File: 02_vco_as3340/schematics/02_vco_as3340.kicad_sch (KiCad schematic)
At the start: 23 parts, among them J1 FM IN, J10 Outputs, J11 SQUARE OUT, J12 SAW OUT, J13 TRIANGLE OUT, J14 SINE OUT, J2 PWM CV IN, J3 SYNC IN, J4 1VO IN, J5 Tuning, J6 Sync Mode, J7 FM & PWM, J8 Mode Switch, J9 Panel Power, SW1 SW_Rotary_1x4, SW2 SW_SPDT

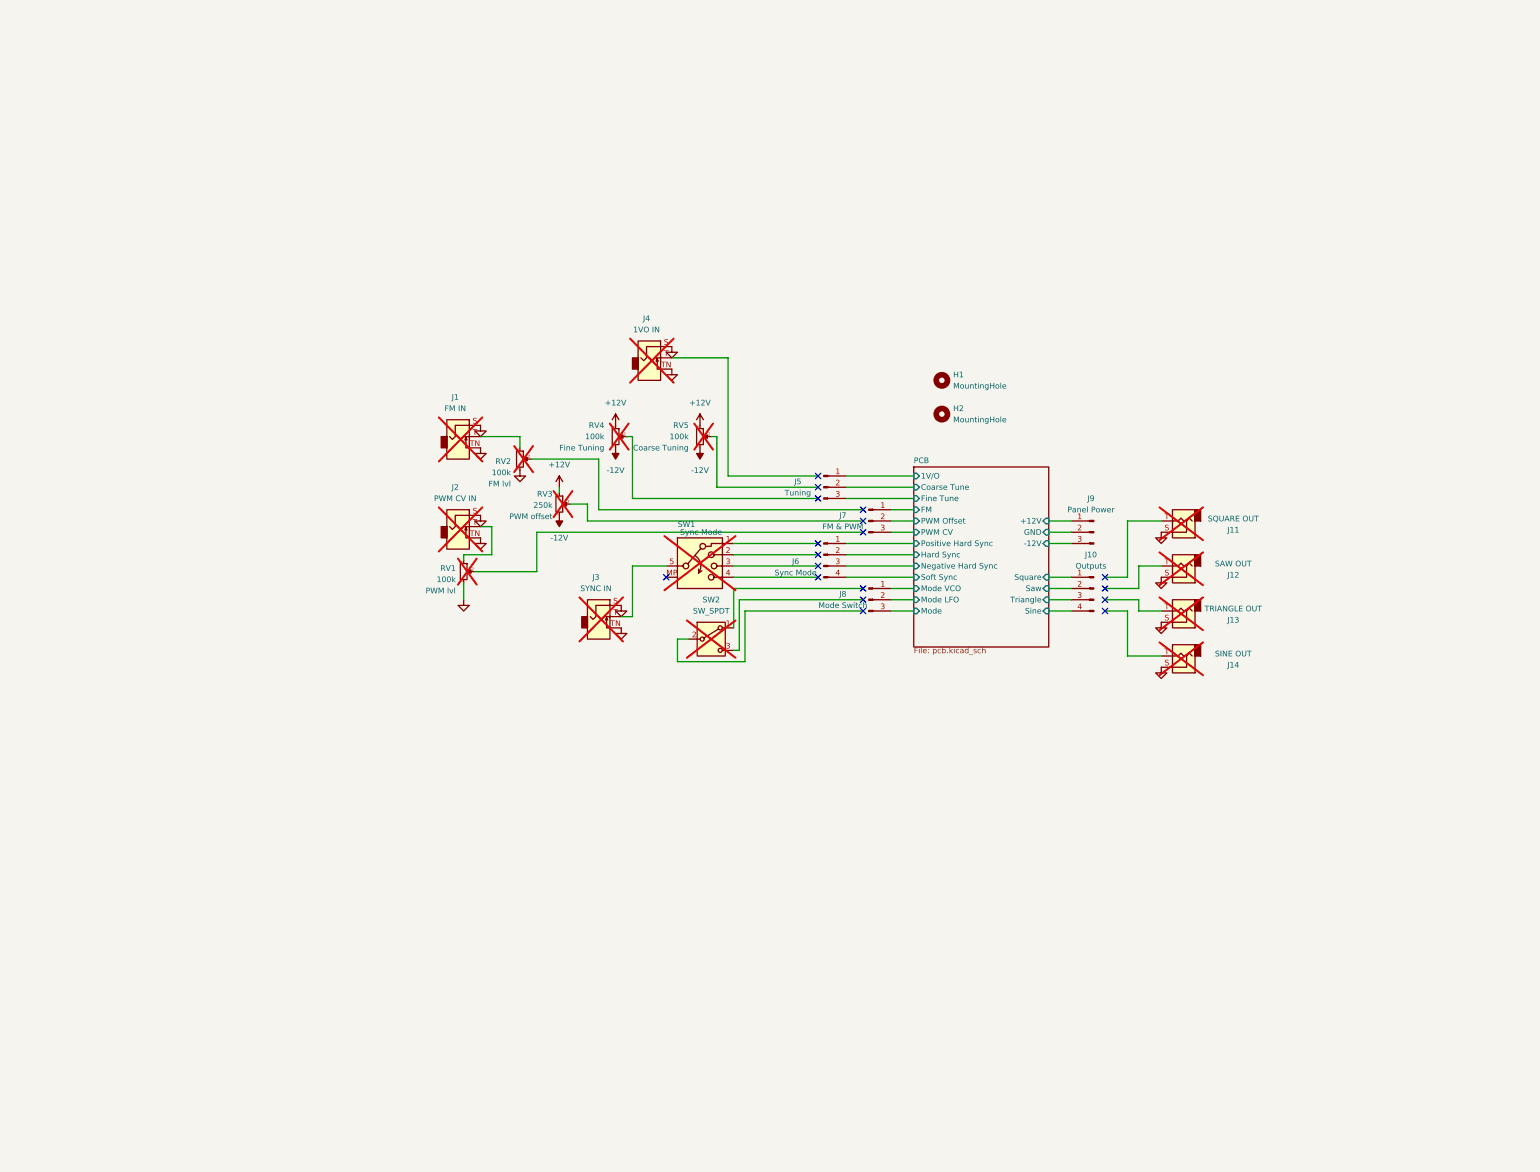
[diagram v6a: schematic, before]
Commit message: split 02 into subboard
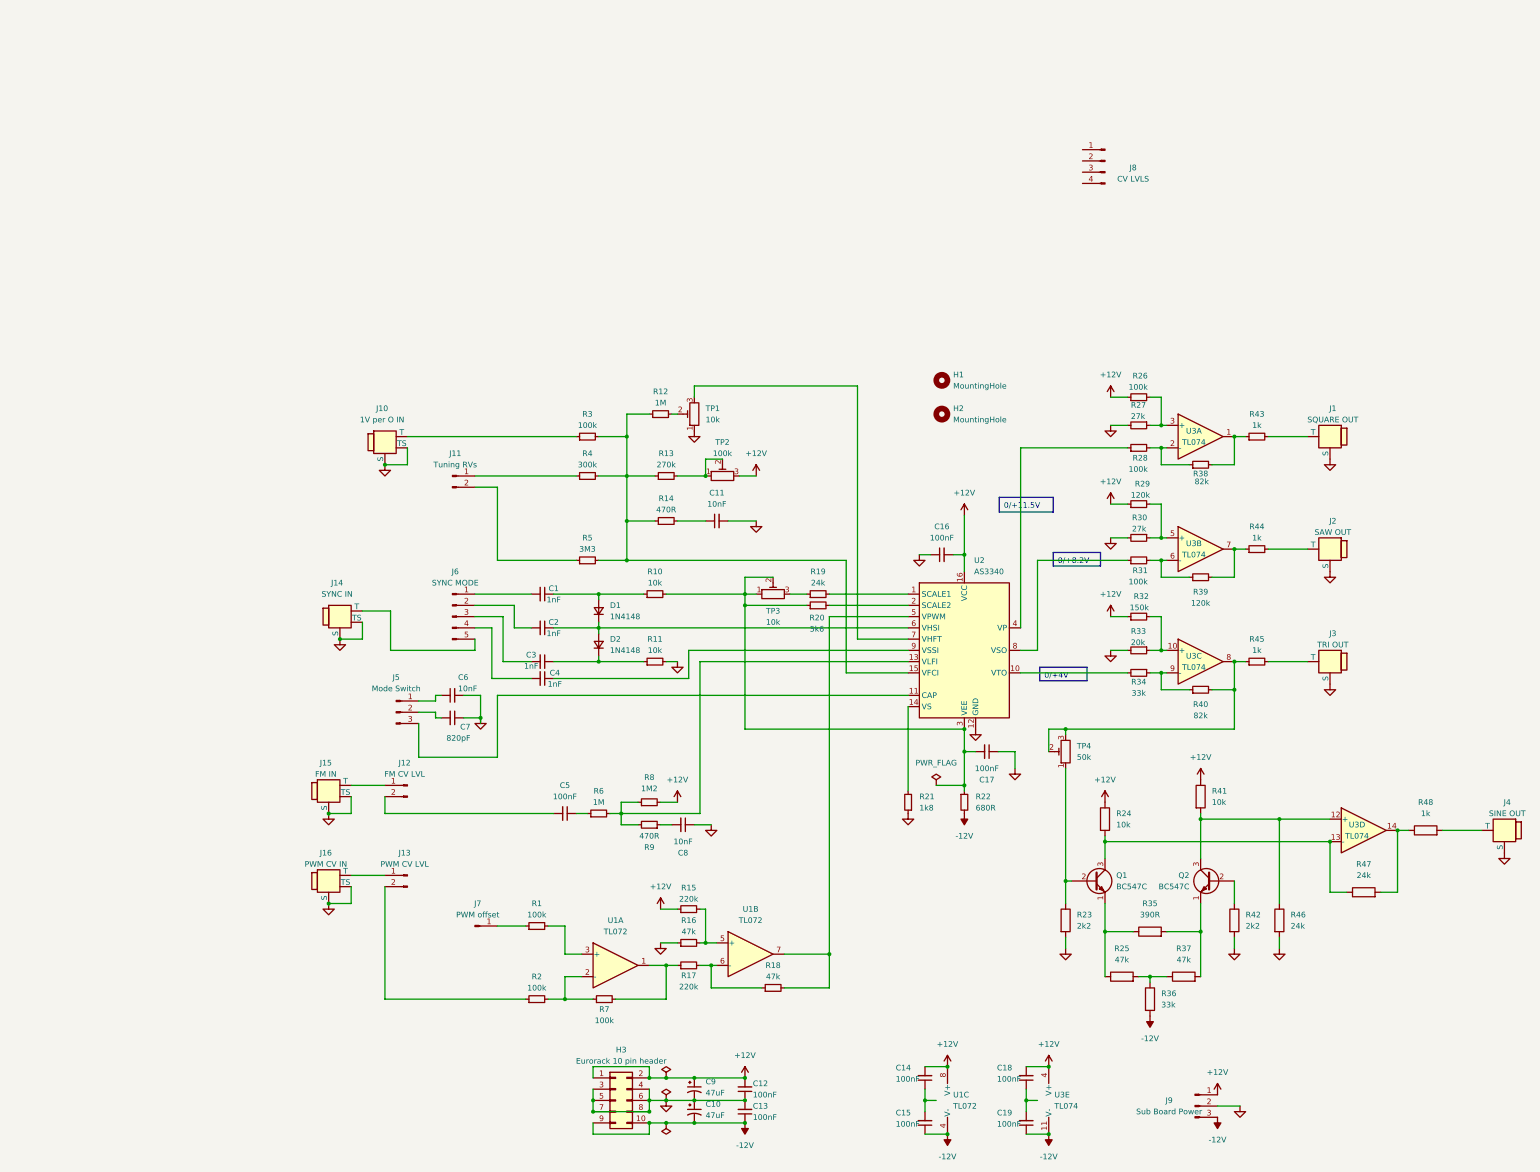
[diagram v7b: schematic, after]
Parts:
- removed J1: FM IN, symbol Connector_Audio:AudioJack2_SwitchT
- removed J10: Outputs, Connector_PinHeader_2.54mm:PinHeader_1x04_P2.54mm_Vertical, symbol Connector:Conn_01x04_Pin
- removed J11: SQUARE OUT, symbol Connector_Audio:AudioJack2
- removed J12: SAW OUT, symbol Connector_Audio:AudioJack2
- removed J13: TRIANGLE OUT, symbol Connector_Audio:AudioJack2
- removed J14: SINE OUT, symbol Connector_Audio:AudioJack2
- removed J2: PWM CV IN, symbol Connector_Audio:AudioJack2_SwitchT
- removed J3: SYNC IN, symbol Connector_Audio:AudioJack2_SwitchT
- removed J4: 1VO IN, symbol Connector_Audio:AudioJack2_SwitchT
- removed J6: Sync Mode, Connector_PinHeader_2.54mm:PinHeader_1x04_P2.54mm_Vertical, symbol Connector:Conn_01x04_Pin
- removed J7: FM & PWM, Connector_PinHeader_2.54mm:PinHeader_1x03_P2.54mm_Vertical, symbol Connector:Conn_01x03_Pin
- removed J8: Mode Switch, Connector_PinHeader_2.54mm:PinHeader_1x03_P2.54mm_Vertical, symbol Connector:Conn_01x03_Pin
- removed RV1, RV2, RV4, RV5: 100k, symbol Device:R_Potentiometer_Small
- removed RV3: 250k, symbol Device:R_Potentiometer_Small
- removed SW1: SW_Rotary_1x4, symbol Switch:SW_Rotary_1x4_MP
- removed SW2: SW_SPDT, symbol Switch:SW_SPDT
- added C1, C2, C3, C4: 1nF, Capacitor_THT:C_Disc_D6.0mm_W2.5mm_P5.00mm, symbol Device:C_Small
- added C10, C9: 47uF, Capacitor_THT:CP_Radial_D6.3mm_P2.50mm, symbol Device:C_Polarized_Small_US
- added C11, C6, C8: 10nF, Capacitor_THT:C_Disc_D6.0mm_W2.5mm_P5.00mm, symbol Device:C_Small
- added C12, C13, C14, C15, C16, C17, C18, C19, C5: 100nF, Capacitor_THT:C_Disc_D6.0mm_W2.5mm_P5.00mm, symbol Device:C_Small
- added C7: 820pF, Capacitor_THT:C_Disc_D6.0mm_W2.5mm_P5.00mm, symbol Device:C_Small
- added D1, D2: 1N4148, Diode_THT:D_DO-35_SOD27_P7.62mm_Horizontal, symbol Device:D_Small
- added H3: Eurorack 10 pin header, Connector_PinHeader_2.54mm:PinHeader_2x05_P2.54mm_Vertical, symbol Connector_Generic:Conn_02x05_Odd_Even
- added J1: SQUARE OUT, cynthia:6.35 mm jack socket mono, symbol cynthia:6.35_mm_jack_socket_mono
- added J10: 1V per O IN, symbol cynthia:6.35_mm_jack_socket_mono_switched
- added J11: Tuning RVs, Connector_PinHeader_2.54mm:PinHeader_1x02_P2.54mm_Vertical, symbol Connector:Conn_01x02_Pin
- added J12: FM CV LVL, Connector_PinHeader_2.54mm:PinHeader_1x02_P2.54mm_Vertical, symbol Connector:Conn_01x02_Pin
- added J13: PWM CV LVL, Connector_PinHeader_2.54mm:PinHeader_1x02_P2.54mm_Vertical, symbol Connector:Conn_01x02_Pin
- added J14: SYNC IN, symbol cynthia:6.35_mm_jack_socket_mono_switched
- added J15: FM IN, symbol cynthia:6.35_mm_jack_socket_mono_switched
- added J16: PWM CV IN, symbol cynthia:6.35_mm_jack_socket_mono_switched
- added J2: SAW OUT, cynthia:6.35 mm jack socket mono, symbol cynthia:6.35_mm_jack_socket_mono
- added J3: TRI OUT, cynthia:6.35 mm jack socket mono, symbol cynthia:6.35_mm_jack_socket_mono
- added J4: SINE OUT, cynthia:6.35 mm jack socket mono, symbol cynthia:6.35_mm_jack_socket_mono
- added J6: SYNC MODE, Connector_PinHeader_2.54mm:PinHeader_1x05_P2.54mm_Vertical, symbol Connector:Conn_01x05_Pin
- added J7: PWM offset, Connector_PinHeader_2.54mm:PinHeader_1x01_P2.54mm_Vertical, symbol Connector:Conn_01x01_Pin
- added J8: CV LVLS, Connector_PinHeader_2.54mm:PinHeader_1x04_P2.54mm_Vertical, symbol Connector:Conn_01x04_Pin
- added Q1, Q2: BC547C, Package_TO_SOT_THT:TO-92_Inline, symbol Transistor_BJT:2N3904
- added R1, R2, R26, R28, R3, R31, R7: 100k, Resistor_THT:R_Axial_DIN0207_L6.3mm_D2.5mm_P10.16mm_Horizontal, symbol Device:R_Small
- added R10, R11: 10k, Resistor_THT:R_Axial_DIN0207_L6.3mm_D2.5mm_P10.16mm_Horizontal, symbol Device:R_Small
- added R12, R6: 1M, Resistor_THT:R_Axial_DIN0207_L6.3mm_D2.5mm_P10.16mm_Horizontal, symbol Device:R_Small
- added R13: 270k, Resistor_THT:R_Axial_DIN0207_L6.3mm_D2.5mm_P10.16mm_Horizontal, symbol Device:R_Small
- added R14, R9: 470R, Resistor_THT:R_Axial_DIN0207_L6.3mm_D2.5mm_P10.16mm_Horizontal, symbol Device:R_Small
- added R15, R17: 220k, Resistor_THT:R_Axial_DIN0207_L6.3mm_D2.5mm_P10.16mm_Horizontal, symbol Device:R_Small
- added R16, R18: 47k, Resistor_THT:R_Axial_DIN0207_L6.3mm_D2.5mm_P10.16mm_Horizontal, symbol Device:R_Small
- added R19: 24k, Resistor_THT:R_Axial_DIN0207_L6.3mm_D2.5mm_P10.16mm_Horizontal, symbol Device:R_Small
- added R20: 5k6, Resistor_THT:R_Axial_DIN0207_L6.3mm_D2.5mm_P10.16mm_Horizontal, symbol Device:R_Small
- added R21: 1k8, Resistor_THT:R_Axial_DIN0207_L6.3mm_D2.5mm_P10.16mm_Horizontal, symbol Device:R_Small
- added R22: 680R, Resistor_THT:R_Axial_DIN0207_L6.3mm_D2.5mm_P10.16mm_Horizontal, symbol Device:R_Small
- added R23, R42: 2k2, Resistor_THT:R_Axial_DIN0207_L6.3mm_D2.5mm_P10.16mm_Horizontal, symbol Device:R
- added R24, R41: 10k, Resistor_THT:R_Axial_DIN0207_L6.3mm_D2.5mm_P10.16mm_Horizontal, symbol Device:R
- added R25, R37: 47k, Resistor_THT:R_Axial_DIN0207_L6.3mm_D2.5mm_P10.16mm_Horizontal, symbol Device:R
- added R27, R30: 27k, Resistor_THT:R_Axial_DIN0207_L6.3mm_D2.5mm_P10.16mm_Horizontal, symbol Device:R_Small
- added R29, R39: 120k, Resistor_THT:R_Axial_DIN0207_L6.3mm_D2.5mm_P10.16mm_Horizontal, symbol Device:R_Small
- added R32: 150k, Resistor_THT:R_Axial_DIN0207_L6.3mm_D2.5mm_P10.16mm_Horizontal, symbol Device:R_Small
- added R33: 20k, Resistor_THT:R_Axial_DIN0207_L6.3mm_D2.5mm_P10.16mm_Horizontal, symbol Device:R_Small
- added R34: 33k, Resistor_THT:R_Axial_DIN0207_L6.3mm_D2.5mm_P10.16mm_Horizontal, symbol Device:R_Small
- added R35: 390R, Resistor_THT:R_Axial_DIN0207_L6.3mm_D2.5mm_P10.16mm_Horizontal, symbol Device:R
- added R36: 33k, Resistor_THT:R_Axial_DIN0207_L6.3mm_D2.5mm_P10.16mm_Horizontal, symbol Device:R
- added R38, R40: 82k, Resistor_THT:R_Axial_DIN0207_L6.3mm_D2.5mm_P10.16mm_Horizontal, symbol Device:R_Small
- added R4: 300k, Resistor_THT:R_Axial_DIN0207_L6.3mm_D2.5mm_P10.16mm_Horizontal, symbol Device:R_Small
- added R43, R44, R45: 1k, Resistor_THT:R_Axial_DIN0207_L6.3mm_D2.5mm_P10.16mm_Horizontal, symbol Device:R_Small
- added R46, R47: 24k, Resistor_THT:R_Axial_DIN0207_L6.3mm_D2.5mm_P10.16mm_Horizontal, symbol Device:R
- added R48: 1k, Resistor_THT:R_Axial_DIN0207_L6.3mm_D2.5mm_P10.16mm_Horizontal, symbol Device:R
- added R5: 3M3, Resistor_THT:R_Axial_DIN0207_L6.3mm_D2.5mm_P10.16mm_Horizontal, symbol Device:R_Small
- added R8: 1M2, Resistor_THT:R_Axial_DIN0207_L6.3mm_D2.5mm_P10.16mm_Horizontal, symbol Device:R_Small
- added TP1, TP3: 10k, Potentiometer_THT:Potentiometer_Vishay_T73XW_Horizontal, symbol Device:R_Potentiometer_Trim
- added TP2: 100k, Potentiometer_THT:Potentiometer_Vishay_T73XW_Horizontal, symbol Device:R_Potentiometer_Trim
- added TP4: 50k, Potentiometer_THT:Potentiometer_Vishay_T73XW_Horizontal, symbol Device:R_Potentiometer_Trim
- added U1: TL072, Package_DIP:DIP-8_W7.62mm, symbol Amplifier_Operational:TL072
- added U2: AS3340, Package_DIP:DIP-16_W7.62mm, symbol Audio:AS3340
- added U3: TL074, Package_DIP:DIP-14_W7.62mm, symbol Amplifier_Operational:TL074
- J5: value Tuning -> Mode Switch
- J9: value Panel Power -> Sub Board Power
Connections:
- net PCB/+12V is gone; now on net +12V: J9.1 (Pin_1)
- net PCB/-12V is gone; now on net -12V: J9.3 (Pin_3)
- net PCB/GND is gone; now on net GND: J9.2 (Pin_2)
- net +12V: now also C12.2, C14.2, C16.2, C18.2, C9.1, H3.1 (Pin_1), H3.2 (Pin_2), R15.1, R24.1, R26.1, R29.1, R32.1, R41.1, R8.2, TP2.3, U1.8 (V+), U2.16 (VCC), U3.4 (V+)
- net -12V: now also C10.2, C13.1, C15.1, C19.1, H3.10 (Pin_10), H3.9 (Pin_9), R22.2, R36.2, U1.4 (V-), U3.11 (V-)
- net GND: now also C10.1, C11.2, C12.1, C13.2, C16.1, C17.1, C6.2, C7.1, C8.1, C9.2, H3.3 (Pin_3), H3.4 (Pin_4), H3.5 (Pin_5), H3.6 (Pin_6), H3.7 (Pin_7), H3.8 (Pin_8), J1.3 (S), J10.2 (TS), J10.3 (S), J14.2 (TS), J14.3 (S), J15.2 (TS), J15.3 (S), J16.2 (TS), J16.3 (S), J2.3 (S), J3.3 (S), J4.3 (S), R11.2, R16.1, R21.1, R23.2, R27.2, R30.2, R33.2, R42.2, R46.2, TP1.1, U2.12 (GND)
- net PCB/1V/O: no longer names the net of J5.1 (Pin_1)
- net PCB/1V/O: now also C6.1
- net PCB/Coarse Tune: no longer names the net of J5.2 (Pin_2)
- net PCB/Coarse Tune: now also C7.2
- net PCB/Fine Tune: no longer names the net of J5.3 (Pin_3)
- net PCB/Fine Tune: now also U2.11 (CAP)
- new net: R19.2, U2.1 (SCALE1)
- new net: R34.2, U2.10 (VTO)
- new net: R6.2, R8.1, R9.2, U2.13 (VLFI)
- new net: R21.2, U2.14 (VS)
- new net: R12.1, R13.1, R14.1, R3.2, R4.2, R5.2, U2.15 (VFCI)
- new net: R20.2, U2.2 (SCALE2)
- new net: C17.2, R10.2, R20.1, R22.1, TP3.1, TP3.2, U2.3 (VEE)
- new net: R28.1, U2.4 (VP)
- new net: R18.2, U1.7, U2.5 (VPWM)
- new net: C2.1, D1.1 (K), D2.2 (A), U2.6 (VHSI)
- new net: TP1.3, U2.7 (VHFT)
- new net: R31.1, U2.8 (VSO)
- new net: C4.1, U2.9 (VSSI)
- new net: R17.2, R18.1, U1.6 (-)
- new net: J14.1 (T), J6.5 (Pin_5)
- new net: J10.1 (T), R3.1
- new net: R25.2, R36.1, R37.1
- new net: C1.1, D1.2 (A), R10.1
- new net: Q2.2 (B), R42.1
- new net: R32.2, R33.1, U3.10 (+)
- new net: R40.2, R45.1, TP4.2, TP4.3, U3.8
- new net: R34.1, R40.1, U3.9 (-)
- new net: C11.1, R14.2
- new net: R12.2, TP1.2
- new net: C14.1, C15.2
- new net: C4.2, J6.4 (Pin_4)
- new net: R17.1, R7.2, U1.1
- new net: R28.2, R38.1, U3.2 (-)
- new net: R38.2, R43.1, U3.1
- new net: R39.2, R44.1, U3.7
- new net: J2.1 (T), R44.2
- new net: R2.2, R7.1, U1.2 (-)
- new net: R19.1, TP3.3
- new net: J12.1 (Pin_1), J15.1 (T)
- new net: C5.2, J12.2 (Pin_2)
- new net: C18.1, C19.2
- new net: J1.1 (T), R43.2
- new net: J3.1 (T), R45.2
- new net: R15.2, R16.2, U1.5 (+)
- new net: C3.1, D2.1 (K), R11.1
- new net: C3.2, J6.3 (Pin_3)
- new net: R26.2, R27.1, U3.3 (+)
- new net: Q2.1 (E), R35.2, R37.2
- new net: Q2.3 (C), R41.2, R46.1, U3.12 (+)
- new net: R13.2, TP2.1, TP2.2
- new net: Q1.1 (E), R25.1, R35.1
- new net: C2.2, J6.2 (Pin_2)
- new net: Q1.2 (B), R23.1, TP4.1
- new net: R47.2, R48.1, U3.14
- new net: J4.1 (T), R48.2
- new net: Q1.3 (C), R24.2, R47.1, U3.13 (-)
- new net: R29.2, R30.1, U3.5 (+)
- new net: C8.2, R9.1
- new net: R31.2, R39.1, U3.6 (-)
- new net: J11.1 (Pin_1), R4.1
- new net: C1.2, J6.1 (Pin_1)
- new net: J11.2 (Pin_2), R5.1
- new net: J13.2 (Pin_2), R2.1
- new net: R1.2, U1.3 (+)
- new net: J7.1 (Pin_1), R1.1
- new net: C5.1, R6.1
- new net: J13.1 (Pin_1), J16.1 (T)
- no-connect marks 18 -> 0
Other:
- removed sheet PCB

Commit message: made sub board for 02
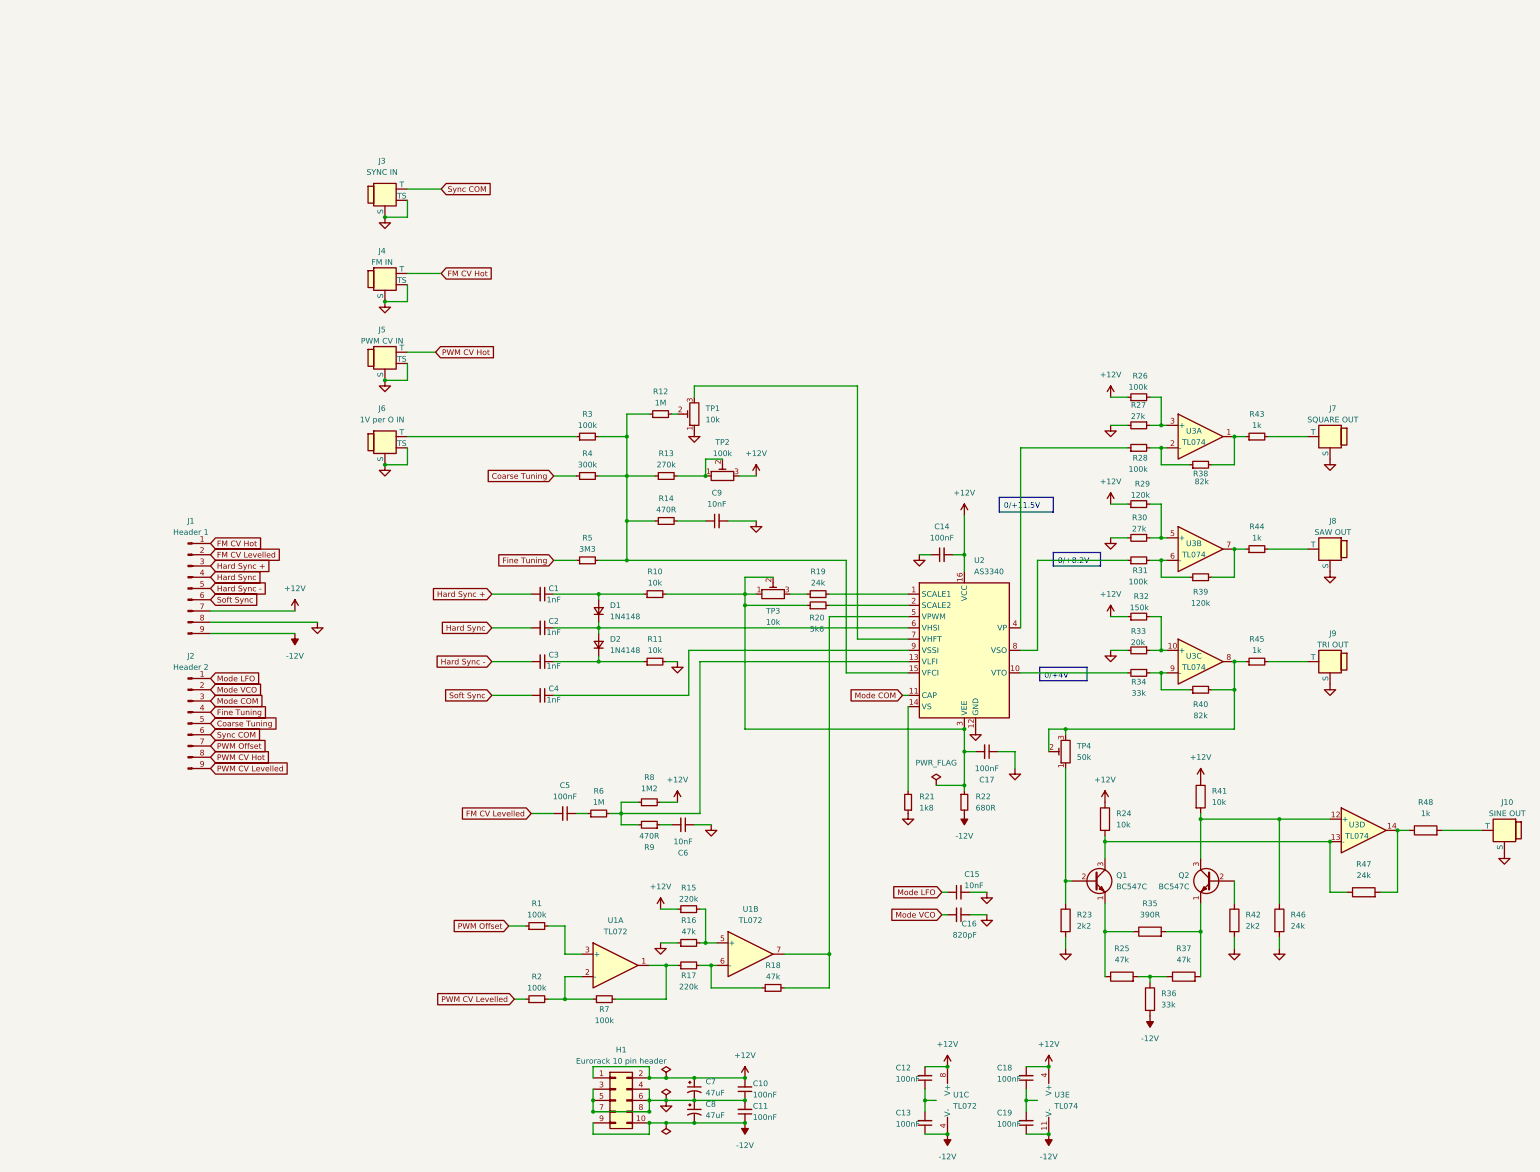
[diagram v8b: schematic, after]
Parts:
- removed H1, H2: MountingHole, MountingHole:MountingHole_3.2mm_M3, symbol Mechanical:MountingHole
- removed J11: Tuning RVs, Connector_PinHeader_2.54mm:PinHeader_1x02_P2.54mm_Vertical, symbol Connector:Conn_01x02_Pin
- removed J12: FM CV LVL, Connector_PinHeader_2.54mm:PinHeader_1x02_P2.54mm_Vertical, symbol Connector:Conn_01x02_Pin
- removed J13: PWM CV LVL, Connector_PinHeader_2.54mm:PinHeader_1x02_P2.54mm_Vertical, symbol Connector:Conn_01x02_Pin
- removed J14: SYNC IN, symbol cynthia:6.35_mm_jack_socket_mono_switched
- removed J16: PWM CV IN, symbol cynthia:6.35_mm_jack_socket_mono_switched
- removed J5: Mode Switch, Connector_PinHeader_2.54mm:PinHeader_1x03_P2.54mm_Vertical, symbol Connector:Conn_01x03_Pin
- removed J6: SYNC MODE, Connector_PinHeader_2.54mm:PinHeader_1x05_P2.54mm_Vertical, symbol Connector:Conn_01x05_Pin
- removed J7: PWM offset, Connector_PinHeader_2.54mm:PinHeader_1x01_P2.54mm_Vertical, symbol Connector:Conn_01x01_Pin
- removed J8: CV LVLS, Connector_PinHeader_2.54mm:PinHeader_1x04_P2.54mm_Vertical, symbol Connector:Conn_01x04_Pin
- removed J9: Sub Board Power, Connector_PinHeader_2.54mm:PinHeader_1x03_P2.54mm_Vertical, symbol Connector:Conn_01x03_Pin
- added J1: Header 1, Connector_PinHeader_2.54mm:PinHeader_1x09_P2.54mm_Vertical, symbol Connector:Conn_01x09_Pin
- added J2: Header 2, Connector_PinHeader_2.54mm:PinHeader_1x09_P2.54mm_Vertical, symbol Connector:Conn_01x09_Pin
- added J3: SYNC IN, cynthia:6.35 mm jack socket mono switched, symbol cynthia:6.35_mm_jack_socket_mono_switched
- added J5: PWM CV IN, cynthia:6.35 mm jack socket mono switched, symbol cynthia:6.35_mm_jack_socket_mono_switched
- J4: renamed from J15; footprint (none) -> cynthia:6.35 mm jack socket mono switched
- J6: renamed from J10; footprint (none) -> cynthia:6.35 mm jack socket mono switched
- renumbered C12 to C10, C13 to C11, C14 to C12, C15 to C13, C16 to C14, C6 to C15, C7 to C16, C8 to C6, C9 to C7, C10 to C8, C11 to C9, H3 to H1, J4 to J10, J1 to J7, J2 to J8, J3 to J9
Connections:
- net +12V: now also J1.7 (Pin_7)
- net -12V: now also J1.9 (Pin_9)
- net GND: now also J10.2 (S), J7.2 (S), J8.2 (S), J9.2 (S), J1.8 (Pin_8), J3.2 (TS), J3.3 (S), J5.2 (TS), J5.3 (S); no longer J10.3 (S), J7.3 (S), J8.3 (S), J9.3 (S)
- net Mode COM: now reaches U2.11 (CAP)
- net Mode COM: now also J2.3 (Pin_3)
- net Soft Sync: now reaches C4.2
- net Soft Sync: now also J1.6 (Pin_6)
- net FM CV Hot: now reaches J4.1 (T)
- net FM CV Hot: now also J1.1 (Pin_1)
- net FM CV Levelled: now reaches C5.2
- net FM CV Levelled: now also J1.2 (Pin_2)
- net Hard Sync -: now reaches C3.2
- net Hard Sync -: now also J1.5 (Pin_5)
- net Hard Sync: now reaches C2.2
- net Hard Sync: now also J1.4 (Pin_4)
- net Coarse Tuning: now reaches R4.1
- net Coarse Tuning: now also J2.5 (Pin_5)
- net Hard Sync +: now reaches C1.2
- net Hard Sync +: now also J1.3 (Pin_3)
- net Mode LFO: now reaches C15.1
- net Mode LFO: now also J2.1 (Pin_1)
- net Mode VCO: now reaches C16.2
- net Mode VCO: now also J2.2 (Pin_2)
- net Fine Tuning: now reaches R5.1
- net Fine Tuning: now also J2.4 (Pin_4)
- net PWM CV Levelled: now reaches R2.1
- net PWM CV Levelled: now also J2.9 (Pin_9)
- net PWM Offset: now reaches R1.1
- net PWM Offset: now also J2.7 (Pin_7)
- new net PWM CV Hot: J2.8 (Pin_8), J5.1 (T)
- new net Sync COM: J2.6 (Pin_6), J3.1 (T)
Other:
- moved on the sheet: C15, C16, C4, J4
